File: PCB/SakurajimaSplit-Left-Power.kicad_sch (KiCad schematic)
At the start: 19 parts, among them J38 USB-C to Host, U10 USBLC6-2SC6, U9 TLV76733DRVR

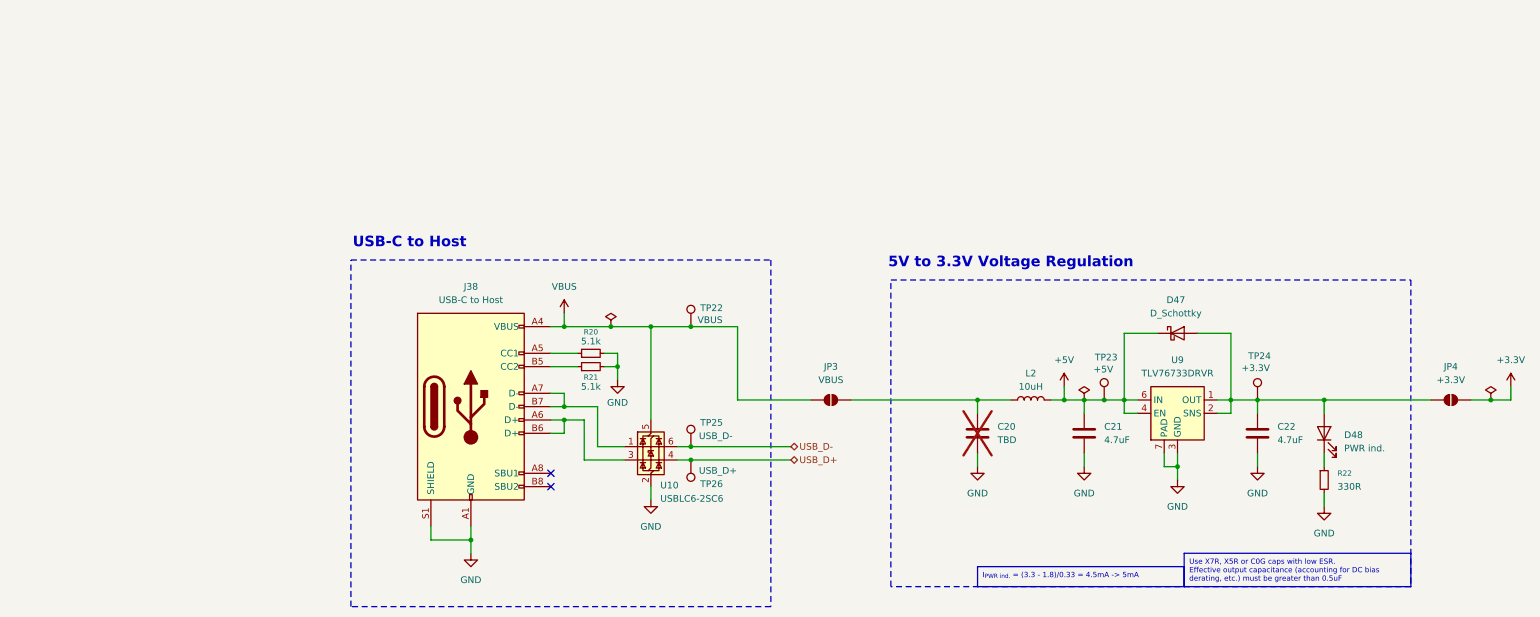
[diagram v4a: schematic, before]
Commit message: feat(pcb): assign all footprints
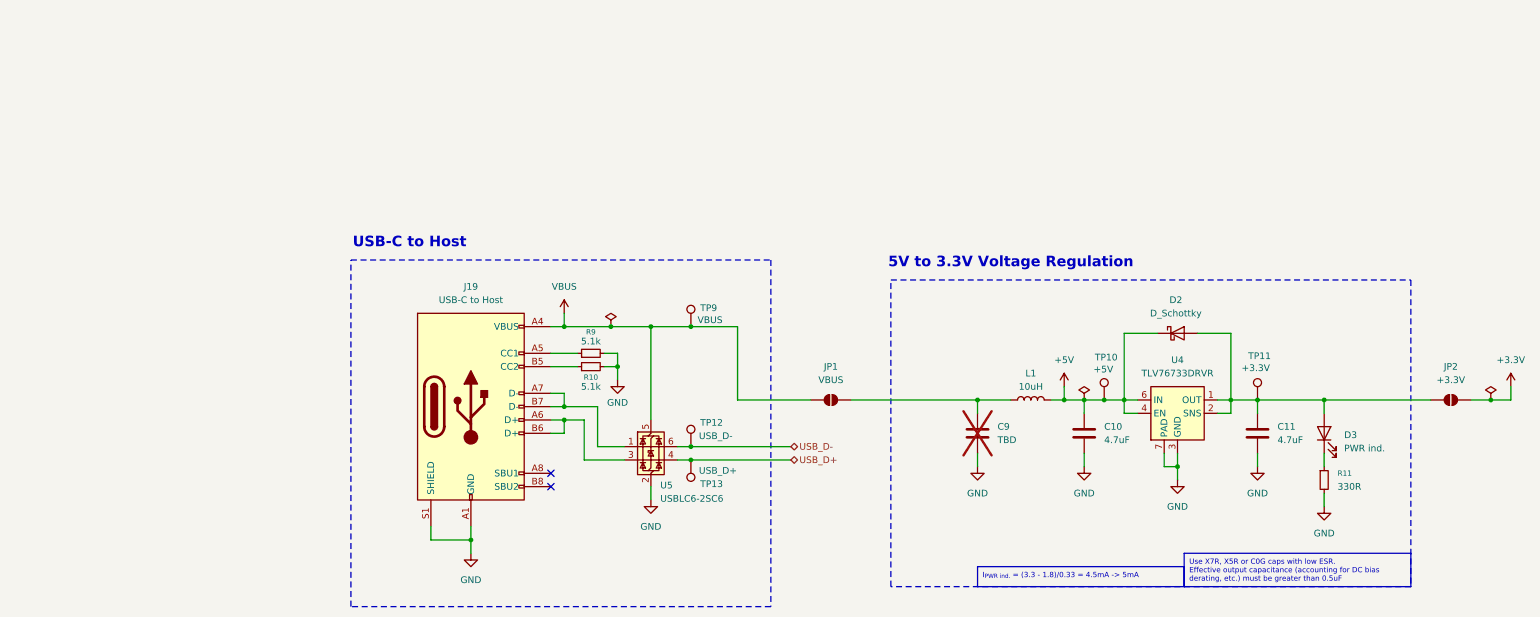
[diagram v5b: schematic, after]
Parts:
- C10: renamed from C21; footprint (none) -> Capacitor_SMD:C_0805_2012Metric
- C11: renamed from C22; footprint (none) -> Capacitor_SMD:C_0805_2012Metric
- C9: renamed from C20; footprint (none) -> Capacitor_SMD:C_0805_2012Metric
- D2: renamed from D47; footprint (none) -> Diode_SMD:D_SOD-123
- D3: renamed from D48; footprint (none) -> LED_SMD:LED_0603_1608Metric
- J19: renamed from J38; footprint (none) -> Connector_USB:USB_C_Receptacle_G-Switch_GT-USB-7010ASV
- JP1: renamed from JP3; footprint (none) -> Jumper:SolderJumper-2_P1.3mm_Open_TrianglePad1.0x1.5mm
- JP2: renamed from JP4; footprint (none) -> Jumper:SolderJumper-2_P1.3mm_Open_TrianglePad1.0x1.5mm
- L1: renamed from L2; footprint (none) -> Inductor_SMD:L_1210_3225Metric
- R10: renamed from R21; footprint (none) -> Resistor_SMD:R_0603_1608Metric
- R11: renamed from R22; footprint (none) -> Resistor_SMD:R_0603_1608Metric
- R9: renamed from R20; footprint (none) -> Resistor_SMD:R_0603_1608Metric
- TP10: renamed from TP23; footprint (none) -> TestPoint:TestPoint_Pad_2.0x2.0mm
- TP11: renamed from TP24; footprint (none) -> TestPoint:TestPoint_Pad_2.0x2.0mm
- TP12: renamed from TP25; footprint (none) -> TestPoint:TestPoint_Pad_2.0x2.0mm
- TP13: renamed from TP26; footprint (none) -> TestPoint:TestPoint_Pad_2.0x2.0mm
- TP9: renamed from TP22; footprint (none) -> TestPoint:TestPoint_Pad_2.0x2.0mm
- renumbered U9 to U4, U10 to U5

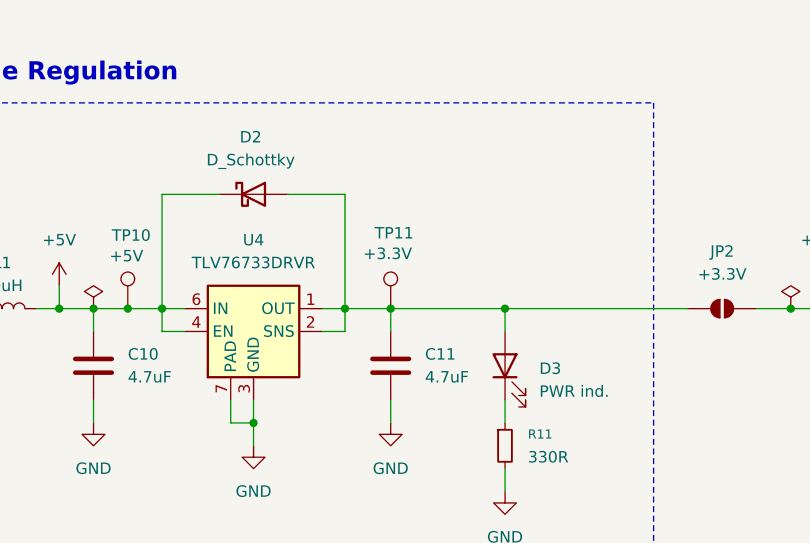
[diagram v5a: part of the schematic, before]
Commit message: fix(sch): fix matrix diode designators not starting from 1
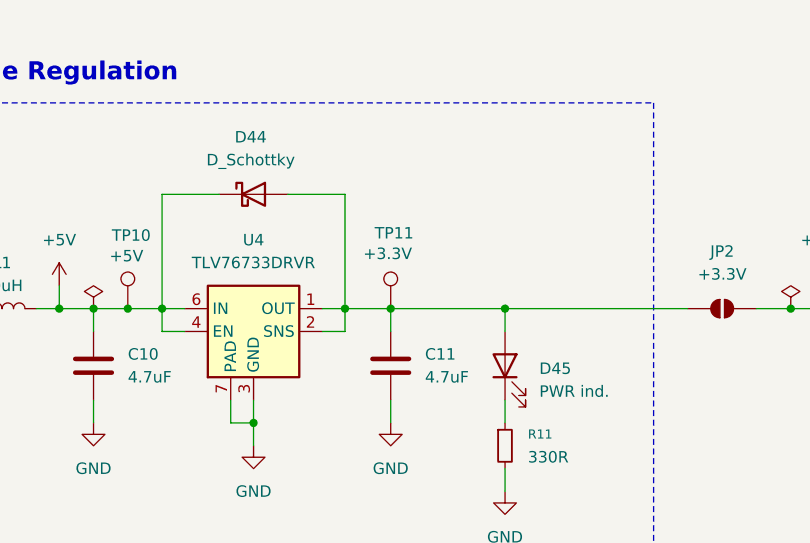
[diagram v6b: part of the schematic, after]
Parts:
- renumbered D2 to D44, D3 to D45
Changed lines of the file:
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@@
 		(dnp no)
 		(fields_autoplaced yes)
-		(property "Reference" "D3"
+		(property "Reference" "D45"
 			(at 295.91 140.0174 90)
 			(effects
@@
 			(project "SakurajimaSplit"
 				(path "/2049b6de-7453-46e1-ab60-70116abff9d6/d08add9a-e5d5-49be-809e-a90adb11436d/38f7f4db-d52f-4e97-96ce-fcb5b455730e"
-					(reference "D3")
+					(reference "D45")
 					(unit 1)
 				)
@@
 		(dnp no)
 		(fields_autoplaced yes)
-		(property "Reference" "D2"
+		(property "Reference" "D44"
 			(at 263.8425 114.3 0)
 			(effects
@@
 			(project "SakurajimaSplit"
 				(path "/2049b6de-7453-46e1-ab60-70116abff9d6/d08add9a-e5d5-49be-809e-a90adb11436d/38f7f4db-d52f-4e97-96ce-fcb5b455730e"
-					(reference "D2")
-					(unit 1)
-				)
+					(reference "D44")
+					(unit 1)
+				)

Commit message: feat(sch): add spi flash, remove rotary encoder, fix footprints
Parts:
- TP10, TP11, TP12, TP13, TP9: footprint TestPoint:TestPoint_Pad_2.0x2.0mm -> Hayata_Lib:TestPoint_Pad_Circular_1.3mm
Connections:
- net VBUS: no longer TP9.1
- net at C9.1, JP1.2 (B), L1.1: now also TP9.1
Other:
- moved on the sheet: TP9
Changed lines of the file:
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@@
 	)
 	(junction
-		(at 171.45 119.38)
+		(at 250.19 133.35)
 		(diameter 0)
 		(color 0 0 0 0)
 	)
 	(junction
-		(at 250.19 133.35)
+		(at 147.32 134.62)
 		(diameter 0)
 		(color 0 0 0 0)
 	)
 	(junction
-		(at 147.32 134.62)
+		(at 242.57 133.35)
 		(diameter 0)
 		(color 0 0 0 0)
 	)
 	(junction
-		(at 242.57 133.35)
+		(at 215.9 133.35)
 		(diameter 0)
 		(color 0 0 0 0)
@@
 	(wire
 		(pts
-			(xy 163.83 119.38) (xy 171.45 119.38)
+			(xy 163.83 119.38) (xy 180.34 119.38)
 		)
 		(stroke
@@
 	(wire
 		(pts
-			(xy 171.45 119.38) (xy 180.34 119.38)
-		)
-		(stroke
-			(width 0)
-			(type default)
-		)
-	)
-	(wire
-		(pts
 			(xy 271.78 135.89) (xy 274.32 135.89)
 		)
@@
 	(wire
 		(pts
-			(xy 201.93 133.35) (xy 226.06 133.35)
+			(xy 201.93 133.35) (xy 215.9 133.35)
 		)
 		(stroke
@@
 	(wire
 		(pts
+			(xy 215.9 133.35) (xy 226.06 133.35)
+		)
+		(stroke
+			(width 0)
+			(type default)
+		)
+	)
+	(wire
+		(pts
 			(xy 147.32 137.16) (xy 147.32 139.7)
 		)
@@
 			)
 		)
-		(property "Footprint" "TestPoint:TestPoint_Pad_2.0x2.0mm"
+		(property "Footprint" "Hayata_Lib:TestPoint_Pad_Circular_1.3mm"
 			(at 284.48 133.35 0)
 			(effects
@@
 			)
 		)
-		(property "Footprint" "TestPoint:TestPoint_Pad_2.0x2.0mm"
+		(property "Footprint" "Hayata_Lib:TestPoint_Pad_Circular_1.3mm"
 			(at 176.53 142.24 0)
 			(effects
@@
 	(symbol
 		(lib_id "Connector:TestPoint")
-		(at 171.45 119.38 0)
+		(at 215.9 133.35 0)
 		(unit 1)
 		(exclude_from_sim no)
@@
 		(dnp no)
 		(property "Reference" "TP9"
-			(at 173.228 115.824 0)
+			(at 217.678 129.794 0)
 			(effects
 				(font
@@
 		)
 		(property "Value" "VBUS"
-			(at 172.72 118.11 0)
+			(at 217.17 132.08 0)
 			(effects
 				(font
@@
 			)
 		)
-		(property "Footprint" "TestPoint:TestPoint_Pad_2.0x2.0mm"
-			(at 176.53 119.38 0)
+		(property "Footprint" "Hayata_Lib:TestPoint_Pad_Circular_1.3mm"
+			(at 220.98 133.35 0)
 			(effects
 				(font
@@
 		)
 		(property "Datasheet" "~"
-			(at 176.53 119.38 0)
+			(at 220.98 133.35 0)
 			(effects
 				(font
@@
 		)
 		(property "Description" "test point"
-			(at 171.45 119.38 0)
+			(at 215.9 133.35 0)
 			(effects
 				(font
@@
 		)
 		(property "Distributor Link" ""
-			(at 171.45 119.38 0)
+			(at 215.9 133.35 0)
 			(effects
 				(font
@@
 		)
 		(property "Manufacturer" ""
-			(at 171.45 119.38 0)
+			(at 215.9 133.35 0)
 			(effects
 				(font
@@
 		)
 		(property "Manufacturer Part No." ""
-			(at 171.45 119.38 0)
+			(at 215.9 133.35 0)
 			(effects
 				(font
@@
 		)
 		(property "Notes" ""
-			(at 171.45 119.38 0)
+			(at 215.9 133.35 0)
 			(effects
 				(font
@@
 			)
 		)
-		(property "Footprint" "TestPoint:TestPoint_Pad_2.0x2.0mm"
+		(property "Footprint" "Hayata_Lib:TestPoint_Pad_Circular_1.3mm"
 			(at 176.53 144.78 0)
 			(effects
@@
 			)
 		)
-		(property "Footprint" "TestPoint:TestPoint_Pad_2.0x2.0mm"
+		(property "Footprint" "Hayata_Lib:TestPoint_Pad_Circular_1.3mm"
 			(at 255.27 133.35 0)
 			(effects

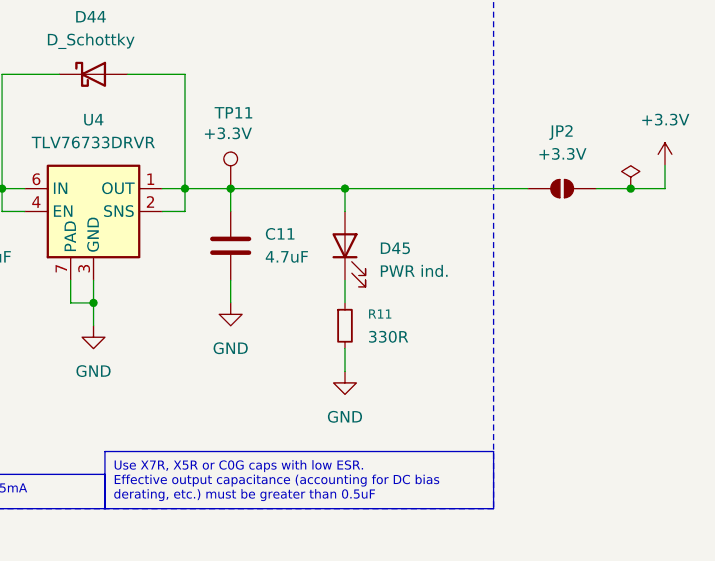
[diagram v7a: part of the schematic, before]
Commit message: fix(sch): swap LEDs with their series resistors
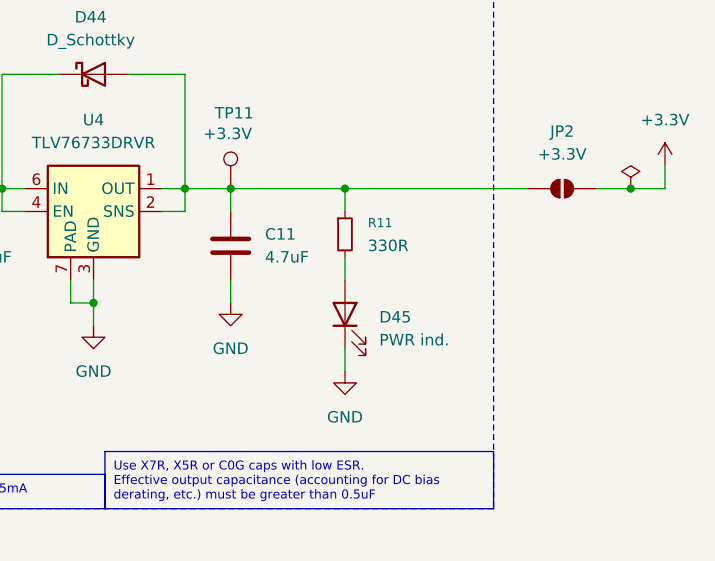
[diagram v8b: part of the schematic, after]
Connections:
- net GND: now also D45.1 (K); no longer R11.2
- net at R11.1: now also C11.1, D44.2 (A), JP2.1 (A), TP11.1, U4.1 (OUT), U4.2 (SNS); no longer D45.1 (K)
- new net: D45.2 (A), R11.2
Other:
- moved on the sheet: D45, R11
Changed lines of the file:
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@@
 	(wire
 		(pts
-			(xy 292.1 143.51) (xy 292.1 146.05)
+			(xy 292.1 140.97) (xy 292.1 143.51)
 		)
 		(stroke
@@
 	(symbol
 		(lib_id "Device:LED")
-		(at 292.1 139.7 90)
+		(at 292.1 147.32 90)
 		(unit 1)
 		(exclude_from_sim no)
@@
 		(fields_autoplaced yes)
 		(property "Reference" "D45"
-			(at 295.91 140.0174 90)
+			(at 295.91 147.6374 90)
 			(effects
 				(font
@@
 		)
 		(property "Value" "PWR ind."
-			(at 295.91 142.5574 90)
+			(at 295.91 150.1774 90)
 			(effects
 				(font
@@
 		)
 		(property "Footprint" "LED_SMD:LED_0603_1608Metric"
-			(at 292.1 139.7 0)
+			(at 292.1 147.32 0)
 			(effects
 				(font
@@
 		)
 		(property "Datasheet" "~"
-			(at 292.1 139.7 0)
+			(at 292.1 147.32 0)
 			(effects
 				(font
@@
 		)
 		(property "Description" "Light emitting diode"
-			(at 292.1 139.7 0)
+			(at 292.1 147.32 0)
 			(effects
 				(font
@@
 		)
 		(property "Sim.Pins" "1=K 2=A"
-			(at 292.1 139.7 0)
+			(at 292.1 147.32 0)
 			(effects
 				(font
@@
 		)
 		(property "Distributor Link" "https://lionelectronic.ir/products/2212-XL-1608UGC-04"
-			(at 292.1 139.7 0)
+			(at 292.1 147.32 0)
 			(effects
 				(font
@@
 		)
 		(property "Manufacturer" "XINGLIGHT"
-			(at 292.1 139.7 0)
+			(at 292.1 147.32 0)
 			(effects
 				(font
@@
 		)
 		(property "Manufacturer Part No." "XL-1608UGC-04"
-			(at 292.1 139.7 0)
+			(at 292.1 147.32 0)
 			(effects
 				(font
@@
 		)
 		(property "Notes" ""
-			(at 292.1 139.7 0)
+			(at 292.1 147.32 0)
 			(effects
 				(font
@@
 	(symbol
 		(lib_id "Device:R_Small")
-		(at 292.1 148.59 0)
+		(at 292.1 138.43 0)
 		(unit 1)
 		(exclude_from_sim no)
@@
 		(fields_autoplaced yes)
 		(property "Reference" "R11"
-			(at 294.64 147.3199 0)
+			(at 294.64 137.1599 0)
 			(effects
 				(font
@@
 		)
 		(property "Value" "330R"
-			(at 294.64 149.8599 0)
+			(at 294.64 139.6999 0)
 			(effects
 				(font
@@
 		)
 		(property "Footprint" "Resistor_SMD:R_0603_1608Metric"
-			(at 292.1 148.59 0)
+			(at 292.1 138.43 0)
 			(effects
 				(font
@@
 		)
 		(property "Datasheet" "~"
-			(at 292.1 148.59 0)
+			(at 292.1 138.43 0)
 			(effects
 				(font
@@
 		)
 		(property "Description" "Resistor, small symbol"
-			(at 292.1 148.59 0)
+			(at 292.1 138.43 0)
 			(effects
 				(font
@@
 		)
 		(property "Distributor Link" "https://lionelectronic.ir/products/1182-SER0603F330R"
-			(at 292.1 148.59 0)
+			(at 292.1 138.43 0)
 			(effects
 				(font
@@
 		)
 		(property "Manufacturer" "VO Sub Brand (ER)"
-			(at 292.1 148.59 0)
+			(at 292.1 138.43 0)
 			(effects
 				(font
@@
 		)
 		(property "Manufacturer Part No." "SER0603F330R"
-			(at 292.1 148.59 0)
+			(at 292.1 138.43 0)
 			(effects
 				(font
@@
 		)
 		(property "Notes" ""
-			(at 292.1 148.59 0)
-			(effects
-				(font
+			(at 292.1 138.43 0)
+			(effects
+				(font
